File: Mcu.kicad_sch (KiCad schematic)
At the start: 21 parts, among them J1 Conn_01x06_Pin, U1 STM32H743ZITx

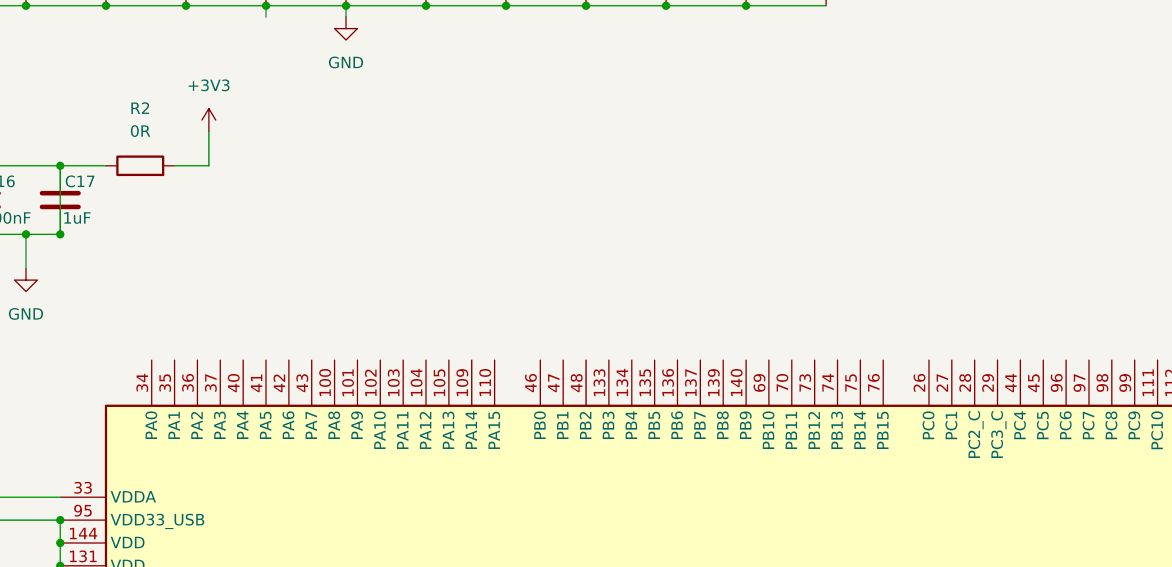
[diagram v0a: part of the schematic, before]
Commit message: Eth güncellendi.
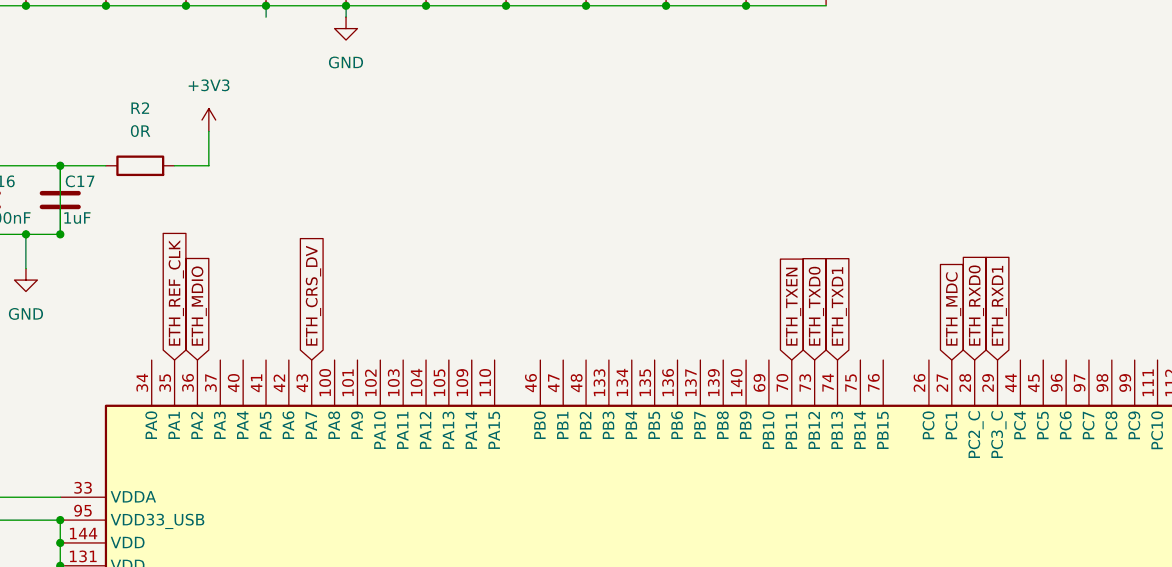
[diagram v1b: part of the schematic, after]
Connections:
- net ETH_MDC: now reaches U1.27 (PC1)
- net ETH_RXD0: now reaches U1.28 (PC2_C)
- net ETH_RXD1: now reaches U1.29 (PC3_C)
- net ETH_REF_CLK: now reaches U1.35 (PA1)
- net ETH_MDIO: now reaches U1.36 (PA2)
- net ETH_CRS_DV: now reaches U1.43 (PA7)
- net ETH_TXEN: now reaches U1.70 (PB11)
- net ETH_TXD0: now reaches U1.73 (PB12)
- net ETH_TXD1: now reaches U1.74 (PB13)

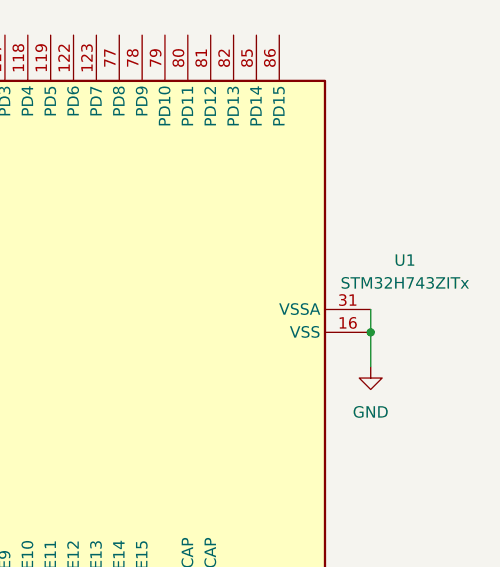
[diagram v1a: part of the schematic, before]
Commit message: Eth güncellendi.
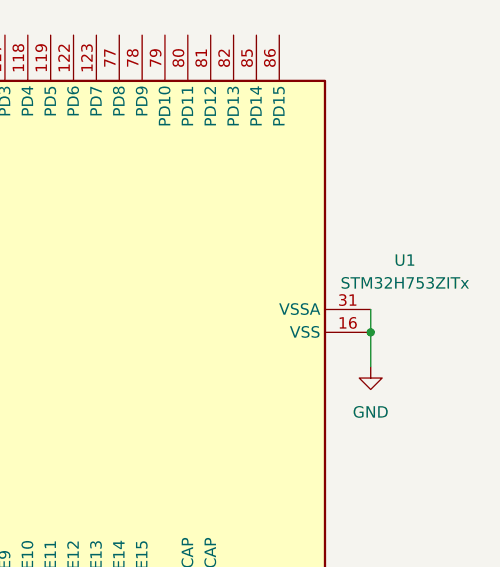
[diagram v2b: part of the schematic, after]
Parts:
- U1: value STM32H743ZITx -> STM32H753ZITx; symbol MCU_ST_STM32H7:STM32H743ZITx -> MCU_ST_STM32H7:STM32H753ZITx
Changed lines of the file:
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@@
+	(wire
+		(pts
+			(xy 218.44 134.62) (xy 218.44 149.86)
+		)
+		(stroke
+			(width 0)
+			(type default)
+		)
+	)
 	(wire
 		(pts
@@
 		(pts
 			(xy 22.86 86.36) (xy 22.86 21.59)
-		)
-		(stroke
-			(width 0)
-			(type default)
-		)
-	)
-	(wire
-		(pts
-			(xy 218.44 134.62) (xy 218.44 149.86)
 		)
 		(stroke
@@
 	)
 	(symbol
-		(lib_id "MCU_ST_STM32H7:STM32H743ZITx")
+		(lib_id "MCU_ST_STM32H7:STM32H753ZITx")
 		(at 144.78 101.6 90)
 		(unit 1)
@@
 			)
 		)
-		(property "Value" "STM32H743ZITx"
+		(property "Value" "STM32H753ZITx"
 			(at 242.57 96.1546 90)
 			(show_name no)
@@
 			)
 		)
-		(property "Datasheet" "https://www.st.com/resource/en/datasheet/stm32h743zi.pdf"
+		(property "Datasheet" "https://www.st.com/resource/en/datasheet/stm32h753zi.pdf"
 			(at 144.78 101.6 0)
 			(hide yes)

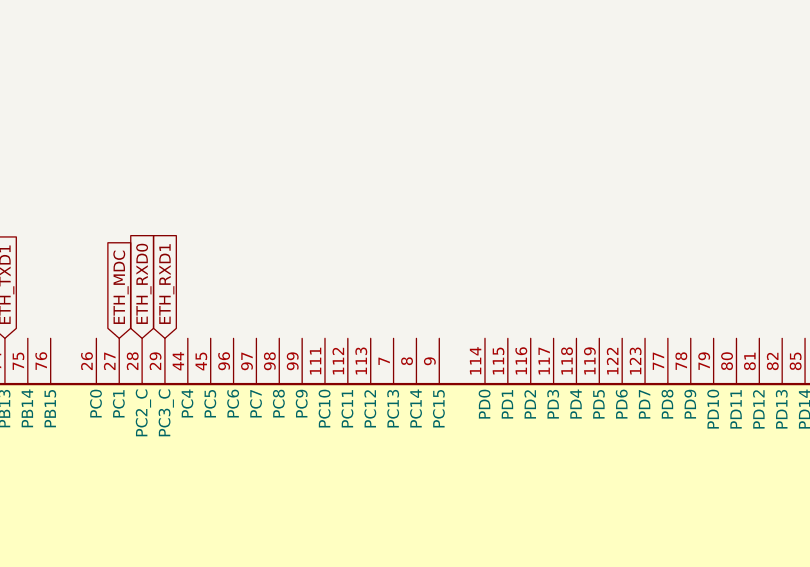
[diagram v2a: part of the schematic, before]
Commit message: Usb Sd arayüzleri eklendi.
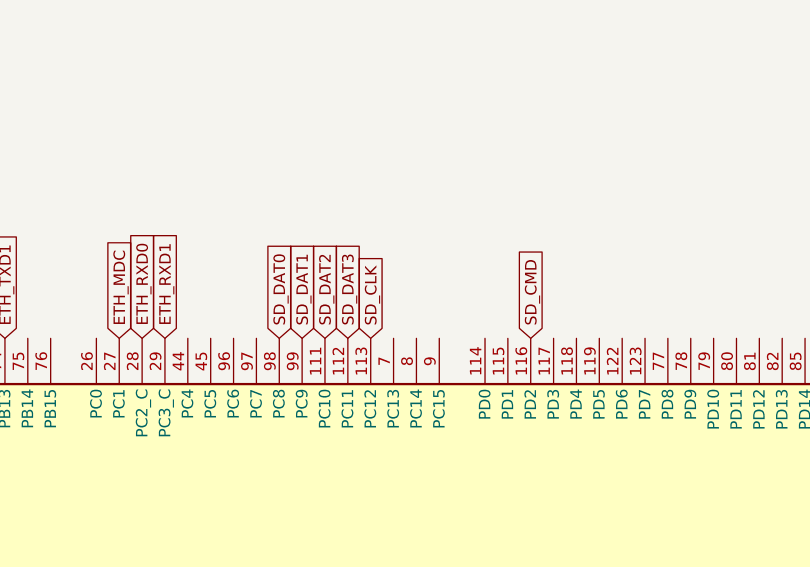
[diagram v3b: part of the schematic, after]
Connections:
- net SD_DAT2: now reaches U1.111 (PC10)
- net SD_DAT3: now reaches U1.112 (PC11)
- net SD_CLK: now reaches U1.113 (PC12)
- net SD_CMD: now reaches U1.116 (PD2)
- net SD_DAT0: now reaches U1.98 (PC8)
- net SD_DAT1: now reaches U1.99 (PC9)
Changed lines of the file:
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@@
+		)
+	)
+	(global_label "SD_CLK"
+		(shape input)
+		(at 177.8 68.58 90)
+		(fields_autoplaced yes)
+		(effects
+			(font
+				(size 1.27 1.27)
+			)
+			(justify left)
+		)
+		(property "Intersheetrefs" "${INTERSHEET_REFS}"
+			(at 177.8 58.5796 90)
+			(hide yes)
+			(show_name no)
+			(do_not_autoplace no)
+			(effects
+				(font
+					(size 1.27 1.27)
+				)
+				(justify left)
+			)
 		)
 	)
@@
 		)
 	)
+	(global_label "SD_DAT3"
+		(shape input)
+		(at 175.26 68.58 90)
+		(fields_autoplaced yes)
+		(effects
+			(font
+				(size 1.27 1.27)
+			)
+			(justify left)
+		)
+		(property "Intersheetrefs" "${INTERSHEET_REFS}"
+			(at 175.26 57.612 90)
+			(hide yes)
+			(show_name no)
+			(do_not_autoplace no)
+			(effects
+				(font
+					(size 1.27 1.27)
+				)
+				(justify left)
+			)
+		)
+	)
 	(global_label "ETH_MDIO"
 		(shape input)
@@
 		)
 	)
+	(global_label "SD_DAT0"
+		(shape input)
+		(at 167.64 68.58 90)
+		(fields_autoplaced yes)
+		(effects
+			(font
+				(size 1.27 1.27)
+			)
+			(justify left)
+		)
+		(property "Intersheetrefs" "${INTERSHEET_REFS}"
+			(at 167.64 57.612 90)
+			(hide yes)
+			(show_name no)
+			(do_not_autoplace no)
+			(effects
+				(font
+					(size 1.27 1.27)
+				)
+				(justify left)
+			)
+		)
+	)
 	(global_label "ETH_TXEN"
 		(shape input)
@@
 			(hide yes)
 			(show_name no)
+			(do_not_autoplace no)
+			(effects
+				(font
+					(size 1.27 1.27)
+				)
+				(justify left)
+			)
+		)
+	)
+	(global_label "SD_DAT1"
+		(shape input)
+		(at 170.18 68.58 90)
+		(fields_autoplaced yes)
+		(effects
+			(font
+				(size 1.27 1.27)
+			)
+			(justify left)
+		)
+		(property "Intersheetrefs" "${INTERSHEET_REFS}"
+			(at 170.18 57.612 90)
+			(hide yes)
+			(show_name no)
+			(do_not_autoplace no)
+			(effects
+				(font
+					(size 1.27 1.27)
+				)
+				(justify left)
+			)
+		)
+	)
+	(global_label "SD_DAT2"
+		(shape input)
+		(at 172.72 68.58 90)
+		(fields_autoplaced yes)
+		(effects
+			(font
+				(size 1.27 1.27)
+			)
+			(justify left)
+		)
+		(property "Intersheetrefs" "${INTERSHEET_REFS}"
+			(at 172.72 57.612 90)
+			(hide yes)
+			(show_name no)
+			(do_not_autoplace no)
+			(effects
+				(font
+					(size 1.27 1.27)
+				)
+				(justify left)
+			)
+		)
+	)
+	(global_label "SD_CMD"
+		(shape input)
+		(at 195.58 68.58 90)
+		(fields_autoplaced yes)
+		(effects
+			(font
+				(size 1.27 1.27)
+			)
+			(justify left)
+		)
+		(property "Intersheetrefs" "${INTERSHEET_REFS}"
+			(at 195.58 58.1563 90)
+			(hide yes)
+			(show_name no)

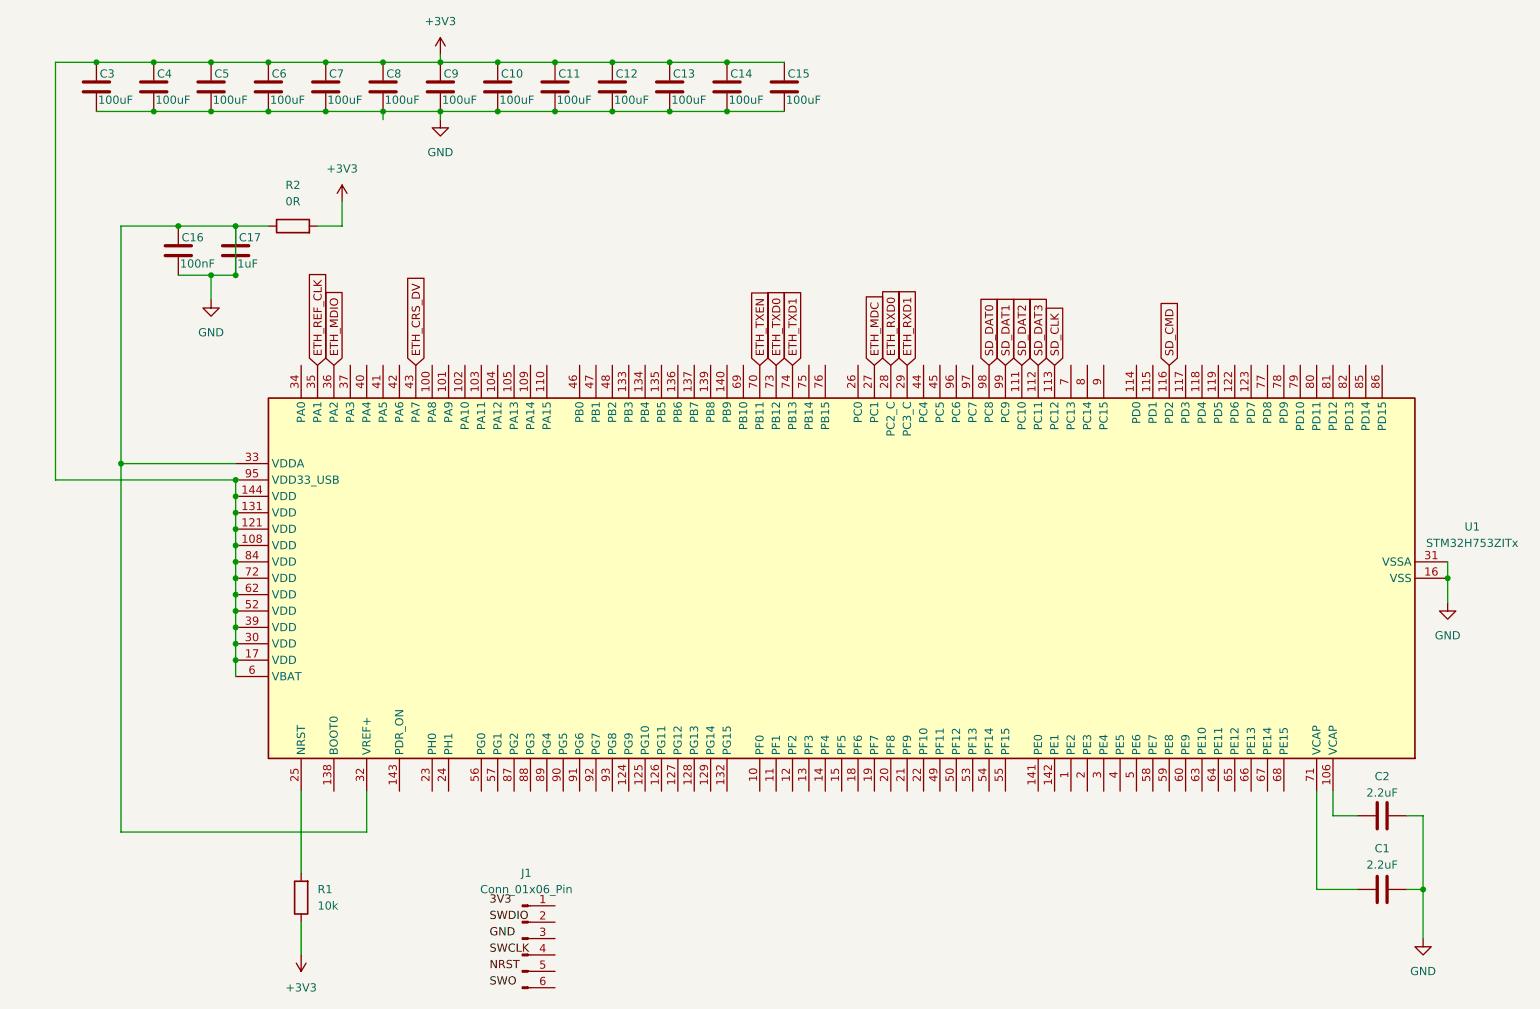
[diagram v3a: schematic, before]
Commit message: Usb düzenlendi.
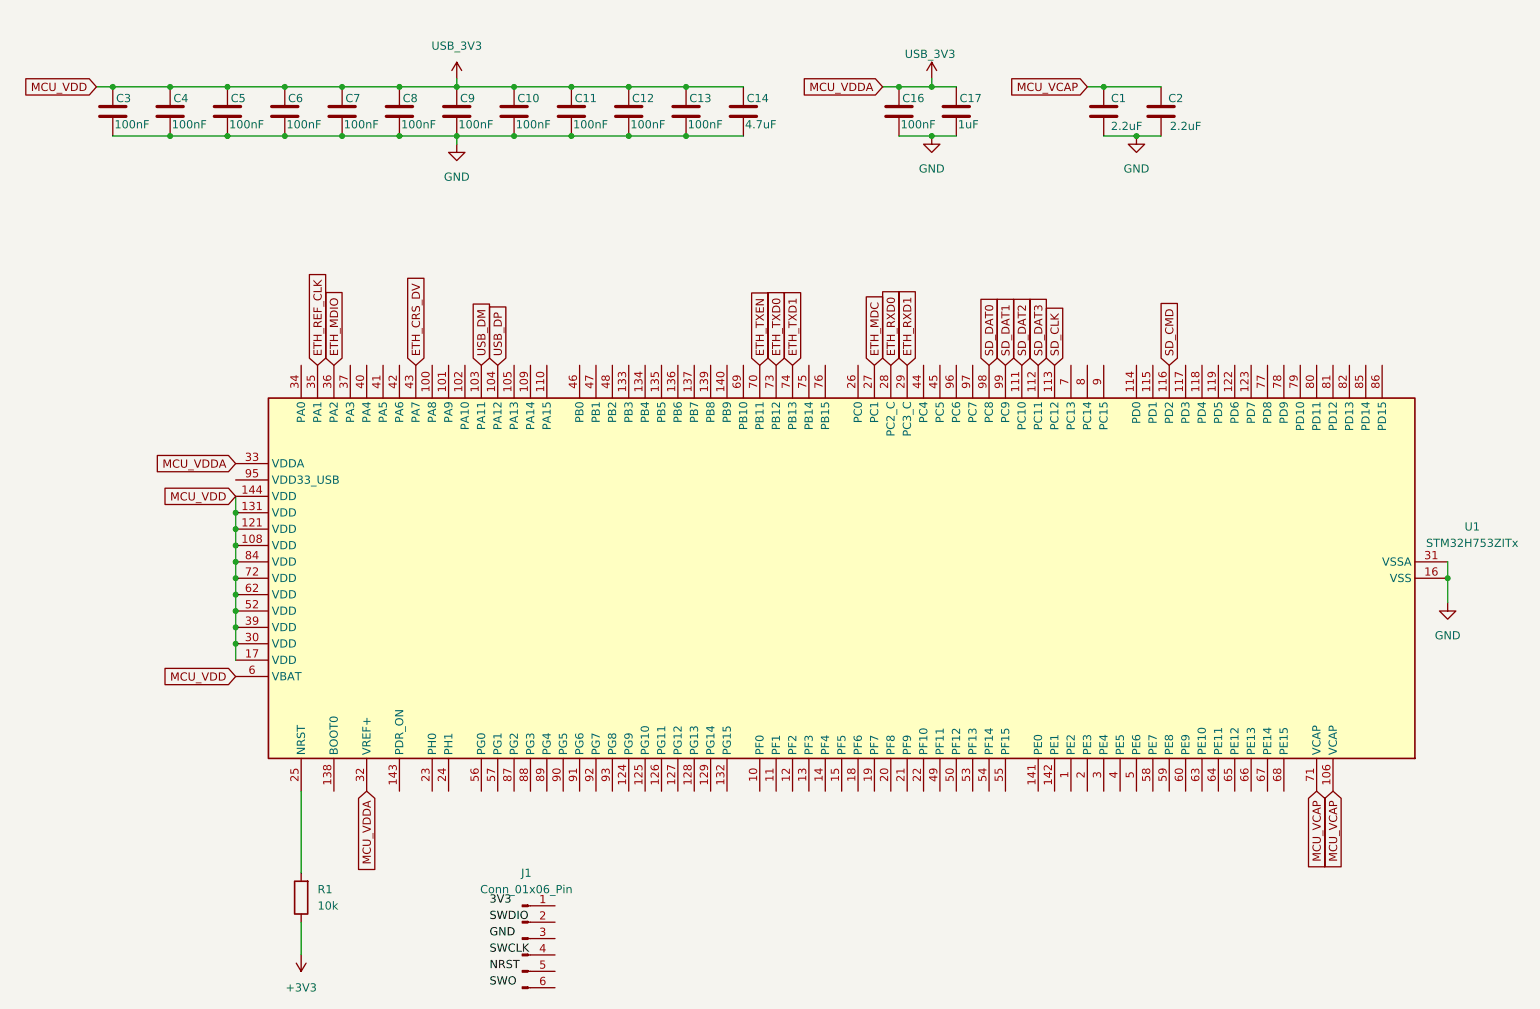
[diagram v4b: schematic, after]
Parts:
- removed C15: 100uF, symbol Device:C
- removed R2: 0R, symbol Device:R
- C10, C11, C12, C13, C3, C4, C5, C6, C7, C8, C9: value 100uF -> 100nF
- C14: value 100uF -> 4.7uF
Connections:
- net +3V3: no longer C10.1, C11.1, C12.1, C13.1, C14.1, C3.1, C4.1, C5.1, C6.1, C7.1, C8.1, C9.1, U1.108 (VDD), U1.121 (VDD), U1.131 (VDD), U1.144 (VDD), U1.17 (VDD), U1.30 (VDD), U1.39 (VDD), U1.52 (VDD), U1.6 (VBAT), U1.62 (VDD), U1.72 (VDD), U1.84 (VDD), U1.95 (VDD33_USB)
- net GND: now also C1.1, C2.1; no longer C1.2, C16.1, C17.1, C2.2, U1.32 (VREF+), U1.33 (VDDA)
- net MCU_VCAP: now reaches U1.106 (VCAP)
- net MCU_VCAP: now also C1.2, C2.2, U1.71 (VCAP); no longer C2.1
- net USB_DM: now reaches U1.103 (PA11)
- net USB_DP: now reaches U1.104 (PA12)
- new net USB_3V3: C10.1, C11.1, C12.1, C13.1, C14.1, C16.1, C17.1, C3.1, C4.1, C5.1, C6.1, C7.1, C8.1, C9.1, U1.108 (VDD), U1.121 (VDD), U1.131 (VDD), U1.144 (VDD), U1.17 (VDD), U1.30 (VDD), U1.32 (VREF+), U1.33 (VDDA), U1.39 (VDD), U1.52 (VDD), U1.6 (VBAT), U1.62 (VDD), U1.72 (VDD), U1.84 (VDD)
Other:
- moved on the sheet: C10, C11, C12, C13, C3, C4, C5, C6, C7, C8, C9
